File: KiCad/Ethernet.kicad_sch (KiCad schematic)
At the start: 24 parts, among them J6 RJMG1BD3B8K1ANR, U16 RTL8019AS, U17 93LC46C, U18 SST39SF040, Y3 20MHz

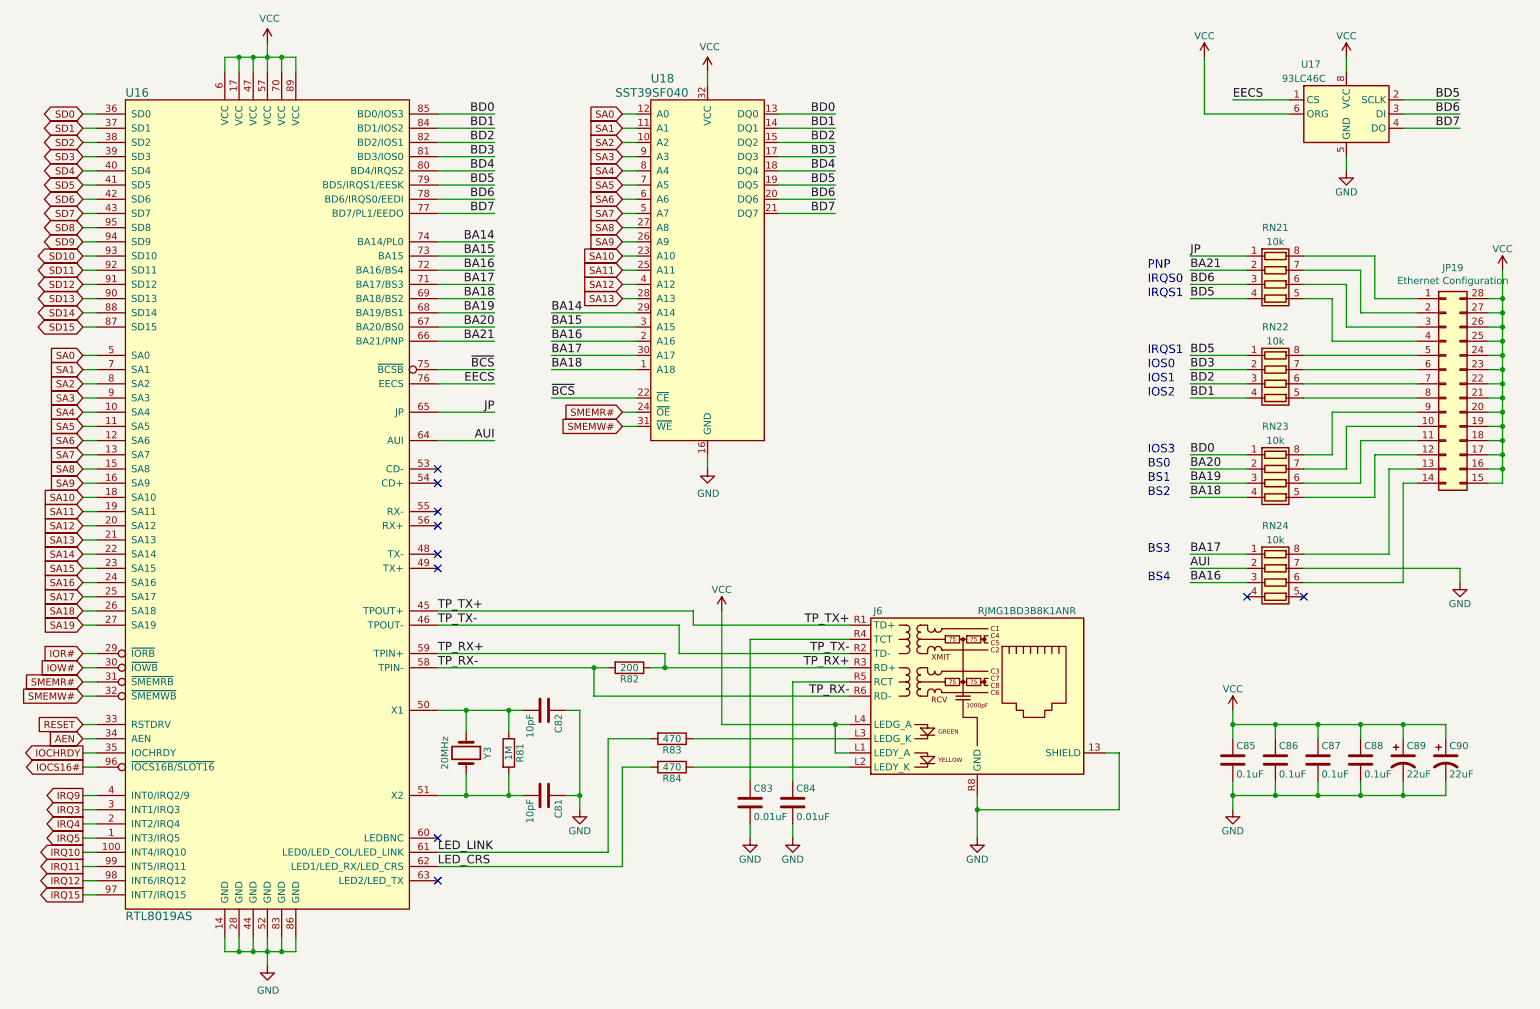
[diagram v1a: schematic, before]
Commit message: Version 0.4: Update chipset connection
Signed-off-by: Sergey Kiselev <skiselev@gmail.com>
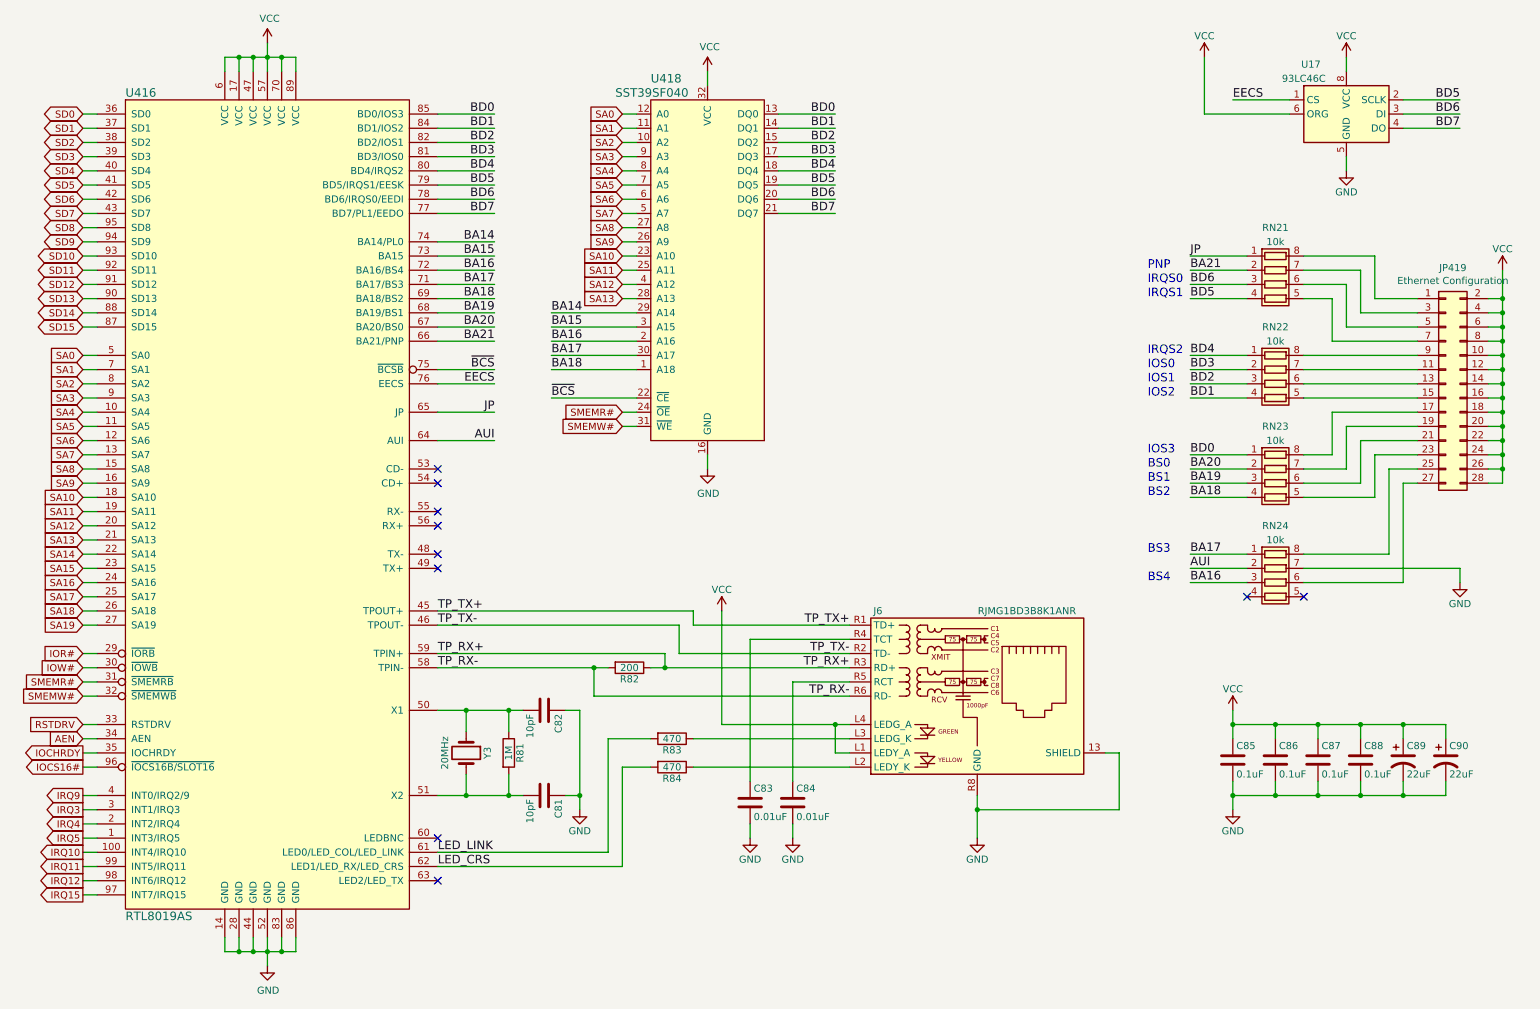
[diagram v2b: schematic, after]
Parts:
- C89, C90: footprint Capacitor_Tantalum_SMD:CP_EIA-3528-15_AVX-H_Pad1.50x2.35mm_HandSolder -> Capacitor_THT:CP_Radial_D5.0mm_P2.00mm; symbol Device:CP1 -> Device:C_Polarized_US
- JP419: renamed from JP19; footprint (none) -> Connector_PinHeader_2.54mm:PinHeader_2x14_P2.54mm_Vertical; symbol Connector_Generic:Conn_02x14_Counter_Clockwise -> Connector_Generic:Conn_02x14_Odd_Even
- U17: footprint Package_SO:SO-8_3.9x4.9mm_P1.27mm -> My_Components:IC_PQFP-100_14x20mm_P0.65mm_Hand_Soldering
- renumbered U16 to U416, U18 to U418
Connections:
- net BD4: now also RN22.1 (R1.1)
- net BD5: no longer RN22.1 (R1.1)
- net VCC: now also JP419.10 (Pin_10), JP419.12 (Pin_12), JP419.14 (Pin_14), JP419.2 (Pin_2), JP419.4 (Pin_4), JP419.6 (Pin_6), JP419.8 (Pin_8); no longer JP419.15 (Pin_15), JP419.17 (Pin_17), JP419.19 (Pin_19), JP419.21 (Pin_21), JP419.23 (Pin_23), JP419.25 (Pin_25), JP419.27 (Pin_27)
- net at RN24.6 (R3.2): now also JP419.27 (Pin_27); no longer JP419.14 (Pin_14)
- net at RN24.8 (R1.2): now also JP419.25 (Pin_25); no longer JP419.13 (Pin_13)
- net at RN21.5 (R4.2): now also JP419.7 (Pin_7); no longer JP419.4 (Pin_4)
- net at RN21.6 (R3.2): now also JP419.5 (Pin_5); no longer JP419.3 (Pin_3)
- net at RN21.7 (R2.2): now also JP419.3 (Pin_3); no longer JP419.2 (Pin_2)
- net at RN22.5 (R4.2): now also JP419.15 (Pin_15); no longer JP419.8 (Pin_8)
- net at RN22.6 (R3.2): now also JP419.13 (Pin_13); no longer JP419.7 (Pin_7)
- net at RN22.7 (R2.2): now also JP419.11 (Pin_11); no longer JP419.6 (Pin_6)
- net at RN22.8 (R1.2): now also JP419.9 (Pin_9); no longer JP419.5 (Pin_5)
- net at RN23.5 (R4.2): now also JP419.23 (Pin_23); no longer JP419.12 (Pin_12)
- net at RN23.6 (R3.2): now also JP419.21 (Pin_21); no longer JP419.11 (Pin_11)
- net at RN23.7 (R2.2): now also JP419.19 (Pin_19); no longer JP419.10 (Pin_10)
- net at RN23.8 (R1.2): now also JP419.17 (Pin_17); no longer JP419.9 (Pin_9)
- net RESET renamed RSTDRV
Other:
- note added: "IRQS2"
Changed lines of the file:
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@@
     (stroke (width 0) (type default) (color 0 0 0 0))
   )
-  (text "IRQS1" (at 215.9 73.66 0)
+  (text "IRQS2" (at 215.9 73.66 0)
     (effects (font (size 1.524 1.524)) (justify left bottom))
   )
@@
     (effects (font (size 1.524 1.524)) (justify right bottom))
   )
-  (label "BD5" (at 223.52 73.66 0)
+  (label "BD4" (at 223.52 73.66 0)
     (effects (font (size 1.524 1.524)) (justify left bottom))
   )
@@
     )
   )
-  (global_label "RESET" (shape input) (at 25.4 139.7 180) (fields_autoplaced)
-    (effects (font (size 1.27 1.27)) (justify right))
-    (property "Intersheet References" "${INTERSHEET_REFS}" (id 0) (at 0 0 0)
-      (effects (font (size 1.27 1.27)) hide)
+  (global_label "RSTDRV" (shape input) (at 25.4 139.7 180) (fields_autoplaced)
+    (effects (font (size 1.27 1.27)) (justify right))
+    (property "Intersheet References" "${INTERSHEET_REFS}" (id 0) (at 16.0001 139.6206 0)
+      (effects (font (size 1.27 1.27)) (justify right) hide)
     )
   )
@@
     (pin "2")
   )
-  (symbol (lib_id "Device:CP1") (at 261.62 146.05 0) (unit 1)
+  (symbol (lib_id "Device:C_Polarized_US") (at 261.62 146.05 0) (unit 1)
     (in_bom yes) (on_board yes)
     (property "Reference" "C89" (id 0) (at 262.255 143.51 0)
@@
       (effects (font (size 1.27 1.27)) (justify left))
     )
-    (property "Footprint" "Capacitor_Tantalum_SMD:CP_EIA-3528-15_AVX-H_Pad1.50x2.35mm_HandSolder" (id 2) (at 261.62 146.05 0)
-      (effects (font (size 1.27 1.27)) hide)
-    )
-    (property "Datasheet" "" (id 3) (at 261.62 146.05 0))
-    (pin "1")
-    (pin "2")
-  )
-  (symbol (lib_id "Device:CP1") (at 269.24 146.05 0) (unit 1)
+    (property "Footprint" "Capacitor_THT:CP_Radial_D5.0mm_P2.00mm" (id 2) (at 261.62 146.05 0)
+      (effects (font (size 1.27 1.27)) hide)
+    )
+    (property "Datasheet" "~" (id 3) (at 261.62 146.05 0)
+      (effects (font (size 1.27 1.27)) hide)
+    )
+    (pin "1")
+    (pin "2")
+  )
+  (symbol (lib_id "Device:C_Polarized_US") (at 269.24 146.05 0) (unit 1)
     (in_bom yes) (on_board yes)
     (property "Reference" "C90" (id 0) (at 269.875 143.51 0)
@@
       (effects (font (size 1.27 1.27)) (justify left))
     )
-    (property "Footprint" "Capacitor_Tantalum_SMD:CP_EIA-3528-15_AVX-H_Pad1.50x2.35mm_HandSolder" (id 2) (at 269.24 146.05 0)
-      (effects (font (size 1.27 1.27)) hide)
-    )
-    (property "Datasheet" "" (id 3) (at 269.24 146.05 0))
+    (property "Footprint" "Capacitor_THT:CP_Radial_D5.0mm_P2.00mm" (id 2) (at 269.24 146.05 0)
+      (effects (font (size 1.27 1.27)) hide)
+    )
+    (property "Datasheet" "~" (id 3) (at 269.24 146.05 0)
+      (effects (font (size 1.27 1.27)) hide)
+    )
     (pin "1")
     (pin "2")
@@
   (symbol (lib_id "my_components:SST39SF040") (at 137.16 58.42 0) (unit 1)
     (in_bom yes) (on_board yes)
-    (property "Reference" "U18" (id 0) (at 127 24.13 0)
+    (property "Reference" "U418" (id 0) (at 127 24.13 0)
       (effects (font (size 1.524 1.524)) (justify left))
     )
@@
   (symbol (lib_id "my_components:RTL8019AS") (at 58.42 100.33 0) (unit 1)
     (in_bom yes) (on_board yes)
-    (property "Reference" "U16" (id 0) (at 33.02 26.67 0)
+    (property "Reference" "U416" (id 0) (at 33.02 26.67 0)
       (effects (font (size 1.524 1.524)) (justify left))
     )
@@
     (property "Reference" "U17" (id 0) (at 245.11 21.59 0))
     (property "Value" "93LC46C" (id 1) (at 243.84 24.13 0))
-    (property "Footprint" "Package_SO:SO-8_3.9x4.9mm_P1.27mm" (id 2) (at 251.46 30.48 0)
+    (property "Footprint" "My_Components:IC_PQFP-100_14x20mm_P0.65mm_Hand_Soldering" (id 2) (at 251.46 30.48 0)
       (effects (font (size 1.27 1.27)) hide)
     )
@@
     (pin "R8")
   )
-  (symbol (lib_id "Connector_Generic:Conn_02x14_Counter_Clockwise") (at 269.24 78.74 0) (unit 1)
-    (in_bom yes) (on_board yes)
-    (property "Reference" "JP19" (id 0) (at 270.51 57.9882 0))
+  (symbol (lib_id "Connector_Generic:Conn_02x14_Odd_Even") (at 269.24 78.74 0) (unit 1)
+    (in_bom yes) (on_board yes)
+    (property "Reference" "JP419" (id 0) (at 270.51 57.9882 0))
     (property "Value" "Ethernet Configuration" (id 1) (at 270.51 60.2996 0))
-    (property "Footprint" "" (id 2) (at 269.24 78.74 0)
-      (effects (font (size 1.27 1.27)) hide)
-    )
+    (property "Footprint" "Connector_PinHeader_2.54mm:PinHeader_2x14_P2.54mm_Vertical" (id 2) (at 269.24 78.74 0)
+      (effects (font (size 1.27 1.27)) hide)
+    )

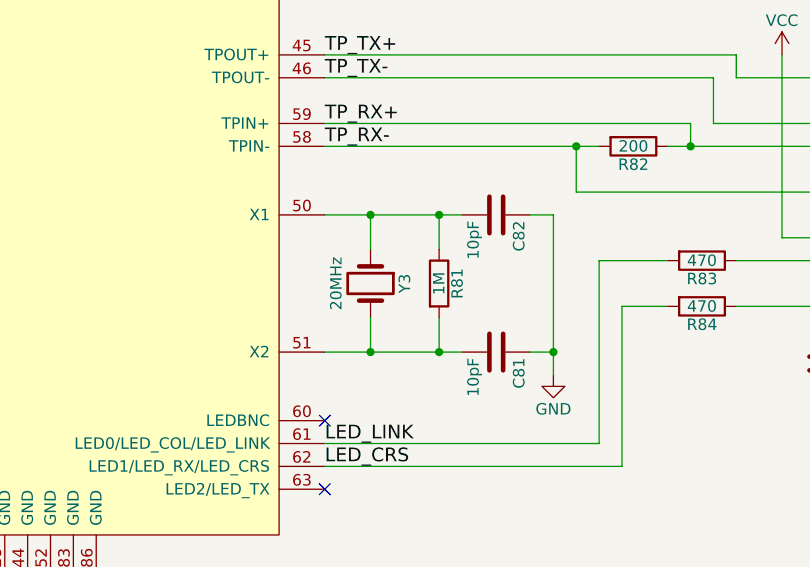
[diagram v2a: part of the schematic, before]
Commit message: More schematic updates. Remove old KiCad files
Signed-off-by: Sergey Kiselev <skiselev@gmail.com>
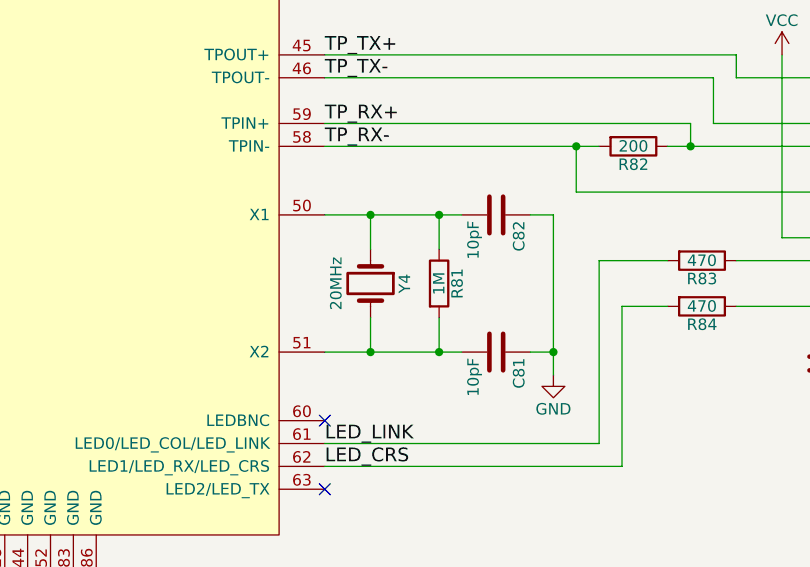
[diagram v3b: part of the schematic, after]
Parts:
- renumbered Y3 to Y4
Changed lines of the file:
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@@
   (symbol (lib_id "Device:Crystal") (at 93.98 144.78 270) (unit 1)
     (in_bom yes) (on_board yes)
-    (property "Reference" "Y3" (id 0) (at 97.79 144.78 0))
+    (property "Reference" "Y4" (id 0) (at 97.79 144.78 0))
     (property "Value" "20MHz" (id 1) (at 90.17 144.78 0))
     (property "Footprint" "My_Components:Crystal_HC-49U_Vert" (id 2) (at 93.98 144.78 0)
